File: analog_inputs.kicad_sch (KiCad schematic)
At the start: 34 parts, among them U201 74HC595

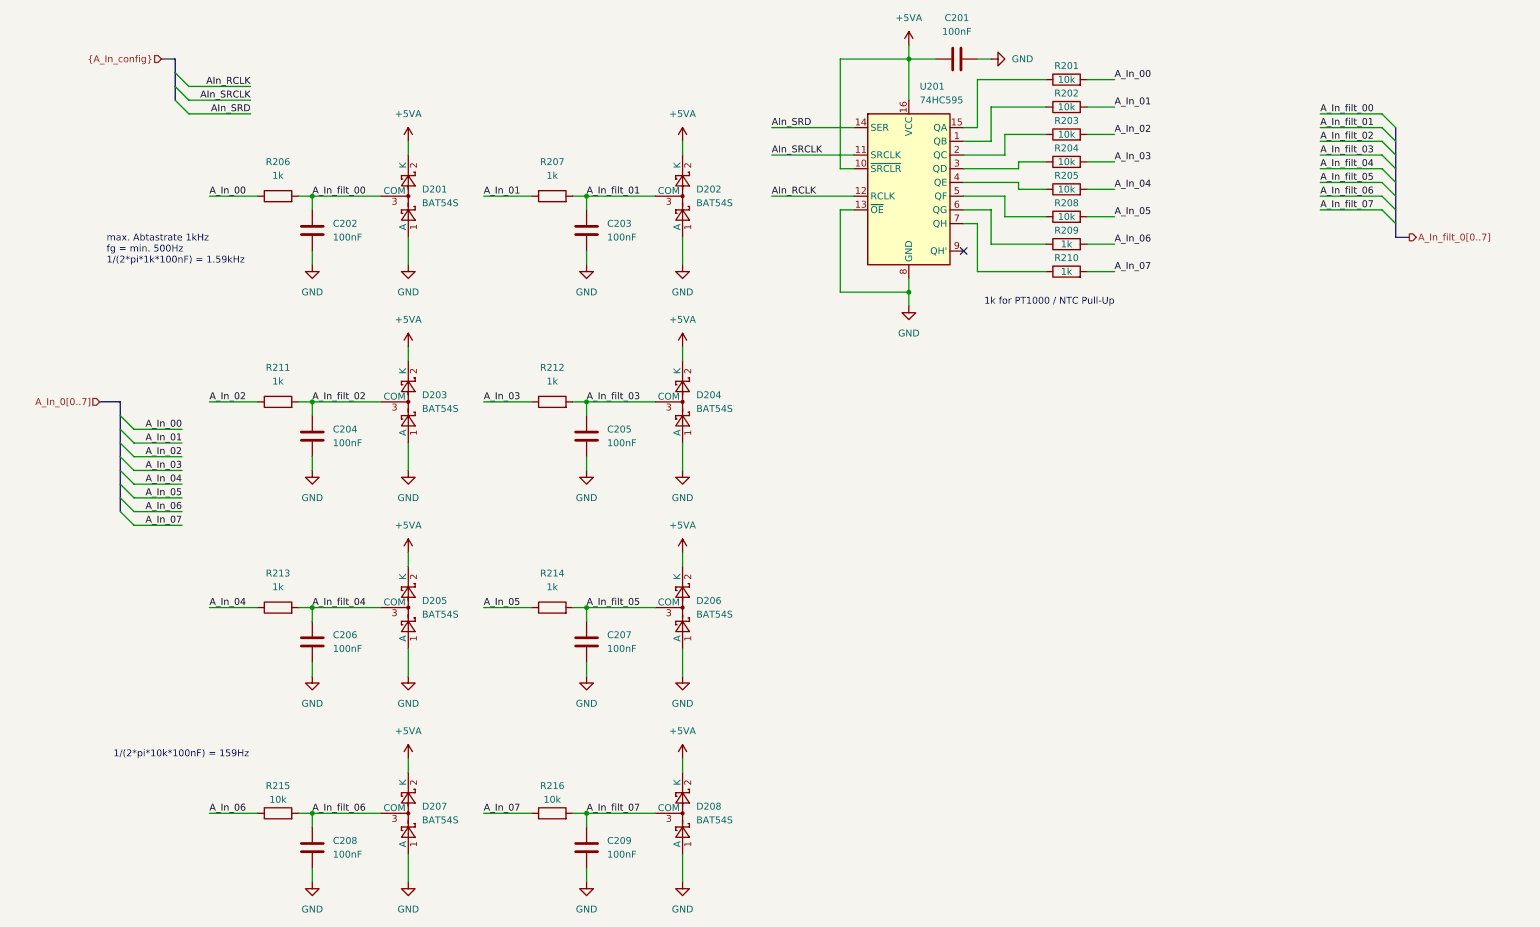
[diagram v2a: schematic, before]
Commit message: hierarchical sheets for digital I/O and replaced power supply jumpers with relays
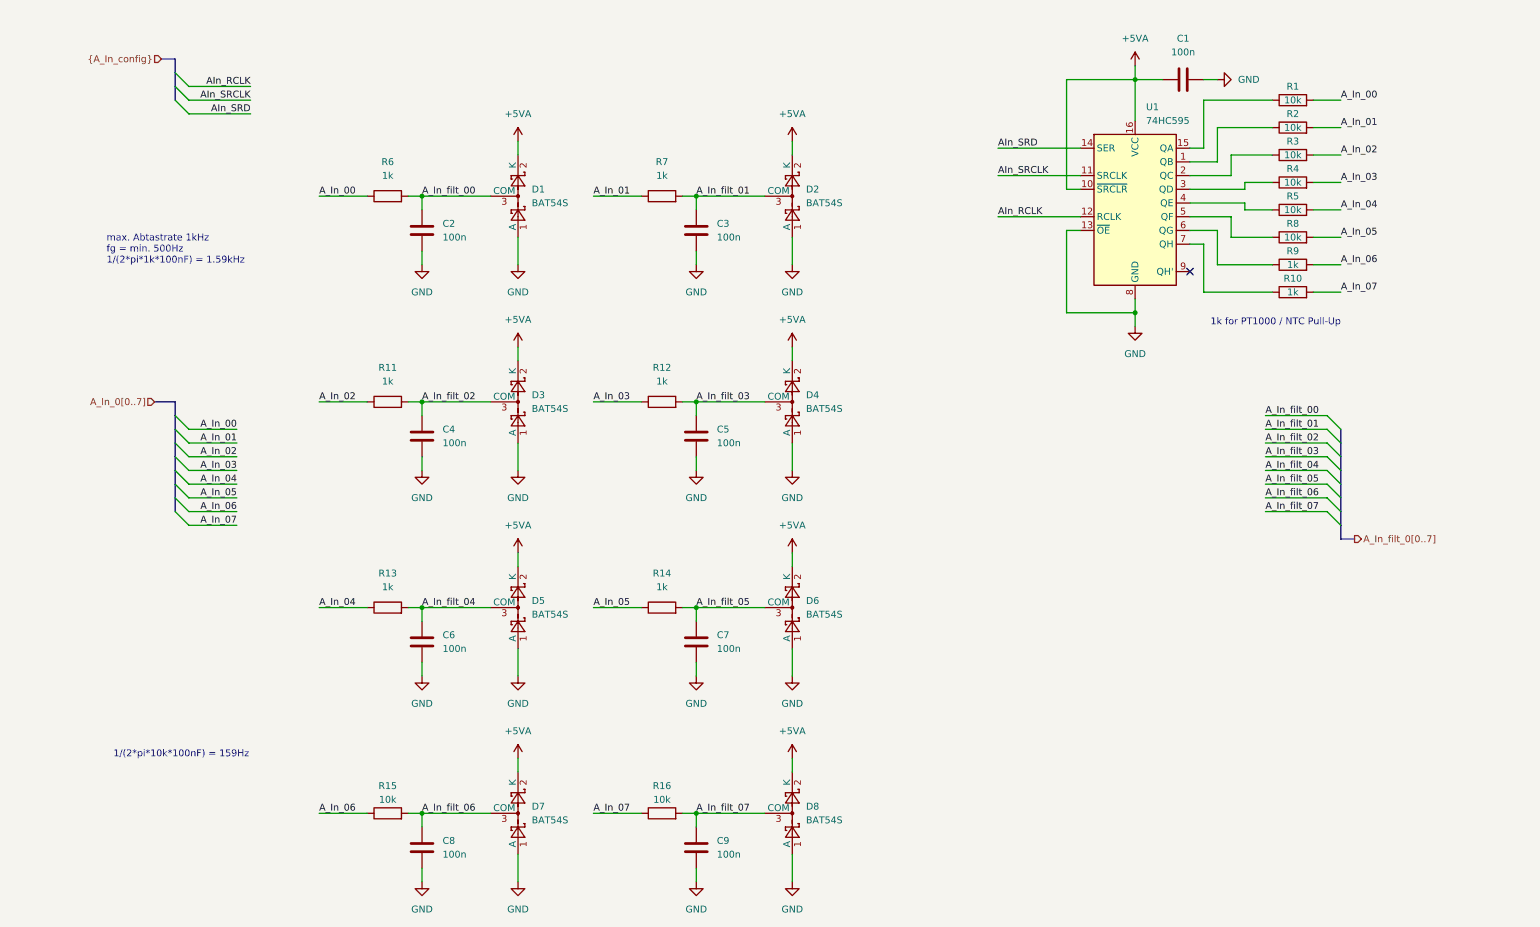
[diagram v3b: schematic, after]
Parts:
- C1: renamed from C201; value 100nF -> 100n
- C2: renamed from C202; value 100nF -> 100n
- C3: renamed from C203; value 100nF -> 100n
- C4: renamed from C204; value 100nF -> 100n
- C5: renamed from C205; value 100nF -> 100n
- C6: renamed from C206; value 100nF -> 100n
- C7: renamed from C207; value 100nF -> 100n
- C8: renamed from C208; value 100nF -> 100n
- C9: renamed from C209; value 100nF -> 100n
- renumbered D201 to D1, D202 to D2, D203 to D3, D204 to D4, D205 to D5, D206 to D6, D207 to D7, D208 to D8, R201 to R1, R210 to R10, R211 to R11, R212 to R12, R213 to R13, R214 to R14, R215 to R15, R216 to R16, R202 to R2, R203 to R3, R204 to R4, R205 to R5, R206 to R6, R207 to R7, R208 to R8, R209 to R9, U201 to U1
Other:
- moved on the sheet: C1, C2, C3, C4, C5, C6, C7, C8, C9, D1, D2, D3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
